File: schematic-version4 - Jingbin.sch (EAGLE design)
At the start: 54 parts, among them J2 FTDI_DEVICE, M1 WIRELESS-NRF24L01, Q1 8MHz, T1 NMOS, T2 NMOS, T3 NMOS, T4 NMOS, U1 ATMEGA328P_TQFP, U2 GY-521MPU6050

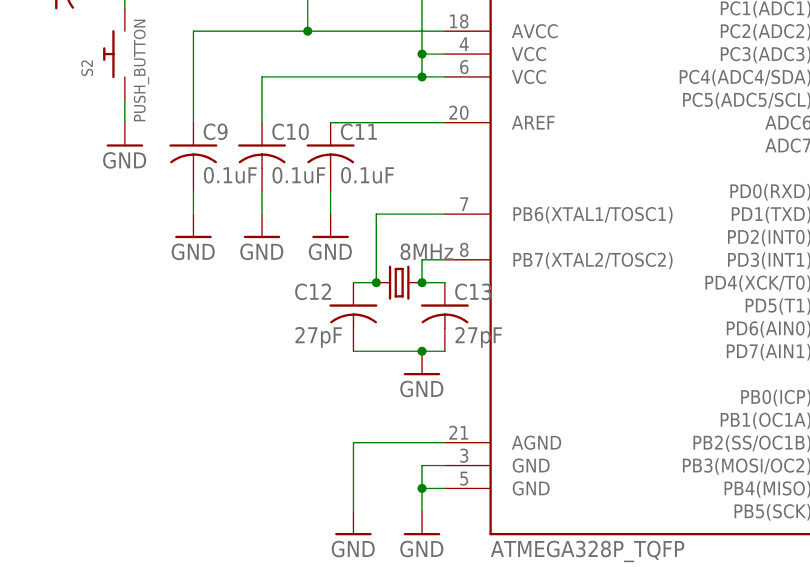
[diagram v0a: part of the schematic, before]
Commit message: Added new crystal
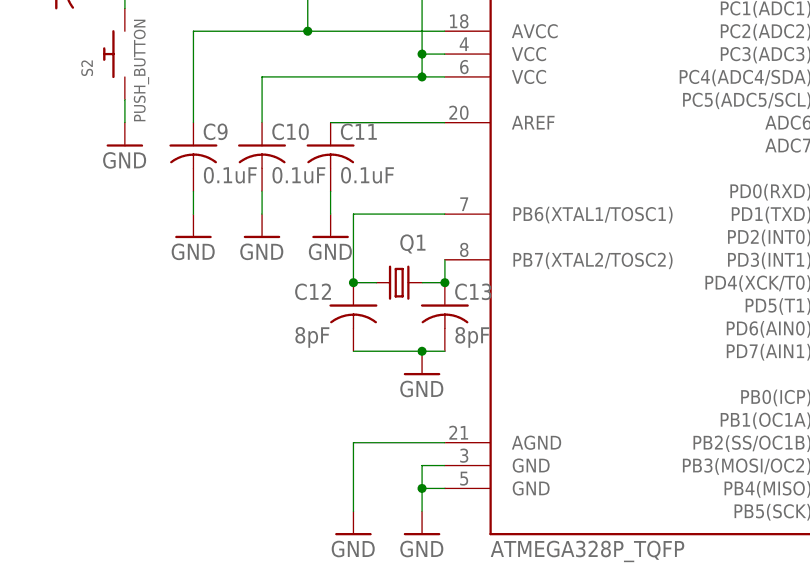
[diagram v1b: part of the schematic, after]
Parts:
- C12, C13: value 27pF -> 8pF
- Q1: value 8MHz -> NX3225GD; device crystal:CSM-7X-DU -> NDK:NX3225GD
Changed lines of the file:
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@@
 <part name="GND31" library="SparkFun" deviceset="GND" device=""/>
 <part name="GND32" library="SparkFun" deviceset="GND" device=""/>
-<part name="C12" library="resistor" library_urn="urn:adsk.eagle:library:348" deviceset="C-US" device="C0603" package3d_urn="urn:adsk.eagle:package:26138/1" value="27pF"/>
-<part name="C13" library="resistor" library_urn="urn:adsk.eagle:library:348" deviceset="C-US" device="C0603" package3d_urn="urn:adsk.eagle:package:26138/1" value="27pF"/>
-<part name="Q1" library="crystal" library_urn="urn:adsk.eagle:library:204" deviceset="CSM-7X-DU" device="" package3d_urn="urn:adsk.eagle:package:12105/1" value="8MHz"/>
+<part name="C12" library="resistor" library_urn="urn:adsk.eagle:library:348" deviceset="C-US" device="C0603" package3d_urn="urn:adsk.eagle:package:26138/1" value="8pF"/>
+<part name="C13" library="resistor" library_urn="urn:adsk.eagle:library:348" deviceset="C-US" device="C0603" package3d_urn="urn:adsk.eagle:package:26138/1" value="8pF"/>
 <part name="R1" library="rcl" library_urn="urn:adsk.eagle:library:334" deviceset="R-US_" device="R0603" package3d_urn="urn:adsk.eagle:package:23555/2" value="820"/>
 <part name="R12" library="rcl" library_urn="urn:adsk.eagle:library:334" deviceset="R-US_" device="R0603" package3d_urn="urn:adsk.eagle:package:23555/2" value="820"/>
@@
 <part name="J2" library="quad" deviceset="FTDI_DEVICE" device=""/>
 <part name="U$2" library="LTC3534" deviceset="LTC3534" device=""/>
+<part name="Q1" library="NDK" deviceset="NX3225GD" device=""/>
 </parts>
 <sheets>
@@
 <attribute name="VALUE" x="176.276" y="66.929" size="1.778" layer="96"/>
 </instance>
-<instance part="Q1" gate="P" x="170.18" y="73.66" smashed="yes">
-<attribute name="VALUE" x="170.18" y="76.2" size="1.778" layer="96"/>
-</instance>
 <instance part="R1" gate="G$1" x="-185.42" y="104.14"/>
 <instance part="R12" gate="G$1" x="-60.96" y="-33.02" rot="R90"/>
@@
 <instance part="J2" gate="G$1" x="-43.18" y="15.24" rot="R180"/>
 <instance part="U$2" gate="G$1" x="-25.4" y="114.3"/>
+<instance part="Q1" gate="G$1" x="170.18" y="73.66" smashed="yes">
+<attribute name="NAME" x="170.18" y="77.216" size="1.778" layer="95"/>
+</instance>
 </instances>
 <busses>
@@
 </segment>
 </net>
-<net name="N$4" class="0">
-<segment>
-<pinref part="C13" gate="G$1" pin="1"/>
-<wire x1="175.26" y1="73.66" x2="172.72" y2="73.66" width="0.1524" layer="91"/>
-<pinref part="U1" gate="U$1" pin="PB7(XTAL2/TOSC2)"/>
-<wire x1="175.26" y1="76.2" x2="172.72" y2="76.2" width="0.1524" layer="91"/>
-<wire x1="172.72" y1="76.2" x2="172.72" y2="73.66" width="0.1524" layer="91"/>
-<pinref part="Q1" gate="P" pin="2"/>
-<junction x="172.72" y="73.66"/>
-</segment>
-</net>
 <net name="SDA" class="0">
 <segment>
@@
 <pinref part="R11" gate="G$1" pin="1"/>
 <pinref part="LED4" gate="G$1" pin="A"/>
-</segment>
-</net>
-<net name="N$1" class="0">
-<segment>
-<pinref part="U1" gate="U$1" pin="PB6(XTAL1/TOSC1)"/>
-<wire x1="175.26" y1="81.28" x2="167.64" y2="81.28" width="0.1524" layer="91"/>
-<wire x1="167.64" y1="81.28" x2="167.64" y2="73.66" width="0.1524" layer="91"/>
-<pinref part="C12" gate="G$1" pin="1"/>
-<wire x1="167.64" y1="73.66" x2="165.1" y2="73.66" width="0.1524" layer="91"/>
-<pinref part="Q1" gate="P" pin="1"/>
-<junction x="167.64" y="73.66"/>
 </segment>
 </net>
@@
 </segment>
 </net>
+<net name="N$1" class="0">
+<segment>
+<pinref part="U1" gate="U$1" pin="PB6(XTAL1/TOSC1)"/>
+<pinref part="C12" gate="G$1" pin="1"/>
+<wire x1="175.26" y1="81.28" x2="165.1" y2="81.28" width="0.1524" layer="91"/>
+<wire x1="165.1" y1="81.28" x2="165.1" y2="73.66" width="0.1524" layer="91"/>
+<pinref part="Q1" gate="G$1" pin="1"/>
+<wire x1="167.64" y1="73.66" x2="165.1" y2="73.66" width="0.1524" layer="91"/>
+<junction x="165.1" y="73.66"/>
+</segment>
+</net>
+<net name="N$4" class="0">
+<segment>
+<pinref part="U1" gate="U$1" pin="PB7(XTAL2/TOSC2)"/>
+<pinref part="C13" gate="G$1" pin="1"/>
+<wire x1="175.26" y1="76.2" x2="175.26" y2="73.66" width="0.1524" layer="91"/>
+<pinref part="Q1" gate="G$1" pin="2"/>
+<wire x1="172.72" y1="73.66" x2="175.26" y2="73.66" width="0.1524" layer="91"/>
+<junction x="175.26" y="73.66"/>
+</segment>
+</net>

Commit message: Change 100uF capacitor size
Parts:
- C1: device rcl:C-USC1210 -> rcl:C-USC1206
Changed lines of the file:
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@@
 <part name="R13" library="resistor" library_urn="urn:adsk.eagle:library:348" deviceset="R-US_" device="R0603" package3d_urn="urn:adsk.eagle:package:26057/1" value="10K"/>
 <part name="R14" library="resistor" library_urn="urn:adsk.eagle:library:348" deviceset="R-US_" device="R0603" package3d_urn="urn:adsk.eagle:package:26057/1" value="10K"/>
-<part name="C1" library="rcl" library_urn="urn:adsk.eagle:library:334" deviceset="C-US" device="C1210" package3d_urn="urn:adsk.eagle:package:23619/2" value="100uF"/>
 <part name="C8" library="rcl" library_urn="urn:adsk.eagle:library:334" deviceset="C-US" device="C0603" package3d_urn="urn:adsk.eagle:package:23616/2" value="0.1uF"/>
 <part name="C9" library="rcl" library_urn="urn:adsk.eagle:library:334" deviceset="C-US" device="C0603" package3d_urn="urn:adsk.eagle:package:23616/2" value="0.1uF"/>
@@
 <part name="U$2" library="LTC3534" deviceset="LTC3534" device=""/>
 <part name="Q1" library="NDK" deviceset="NX3225GD" device=""/>
+<part name="C1" library="rcl" library_urn="urn:adsk.eagle:library:334" deviceset="C-US" device="C1206" package3d_urn="urn:adsk.eagle:package:23618/2" value="100uF"/>
 </parts>
 <sheets>
@@
 <instance part="R13" gate="G$1" x="-193.04" y="-2.54" rot="R90"/>
 <instance part="R14" gate="G$1" x="-144.78" y="-2.54" rot="R90"/>
-<instance part="C1" gate="G$1" x="-147.32" y="116.84"/>
 <instance part="C8" gate="G$1" x="132.08" y="106.68" rot="R90"/>
 <instance part="C9" gate="G$1" x="147.32" y="88.9"/>
@@
 <attribute name="NAME" x="170.18" y="77.216" size="1.778" layer="95"/>
 </instance>
+<instance part="C1" gate="G$1" x="-147.32" y="116.84"/>
 </instances>
 <busses>
